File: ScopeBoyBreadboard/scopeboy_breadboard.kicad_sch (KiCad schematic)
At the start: 7 parts, among them U1 Opamp_Dual

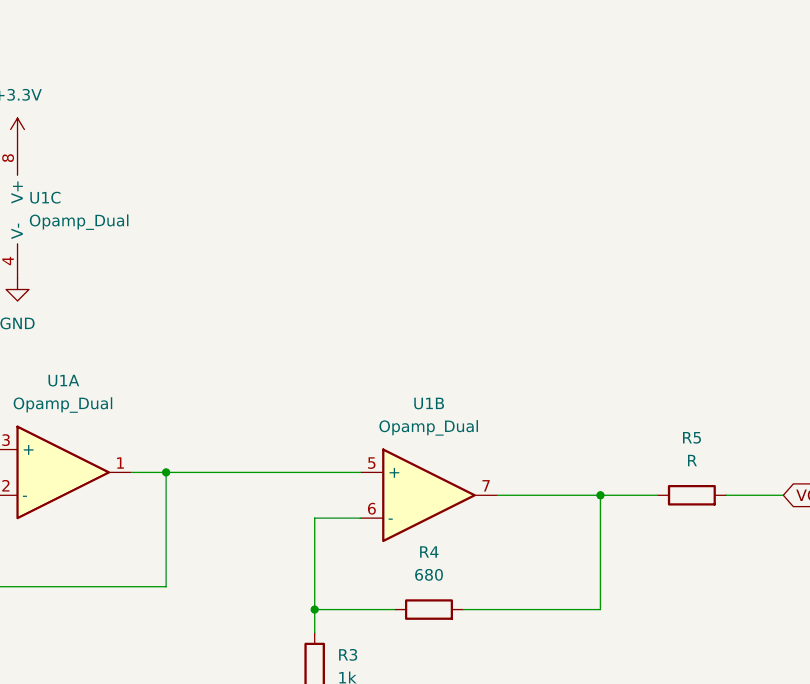
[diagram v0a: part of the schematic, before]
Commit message: Edited schematic, changed default trigger, and working on gain mode
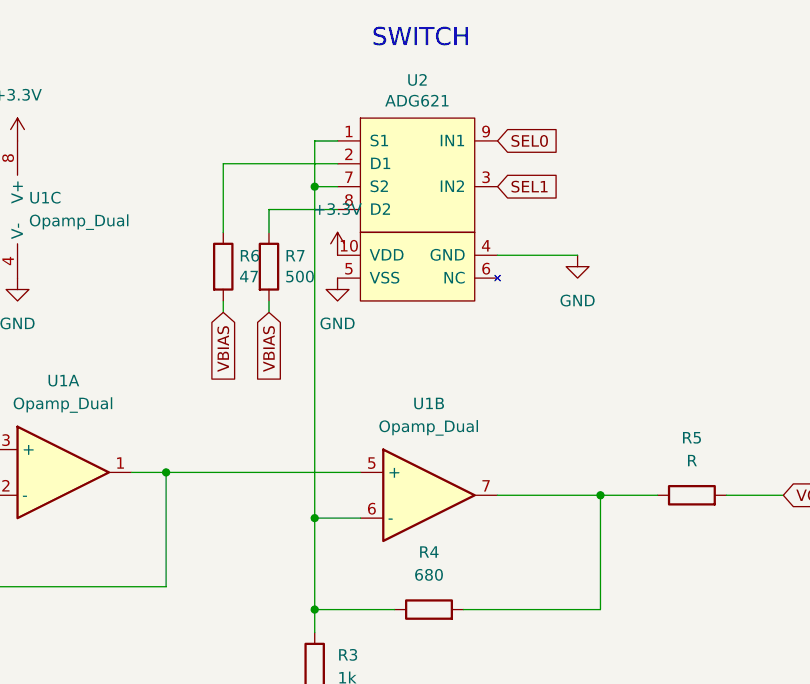
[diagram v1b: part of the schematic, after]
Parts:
- added R6: 47, Resistor_SMD:R_0603_1608Metric, symbol Device:R
- added R7: 500, Resistor_SMD:R_0603_1608Metric, symbol Device:R
- added U2: ADG621, Package_SO:MSOP-10_3x3mm_P0.5mm, symbol rpicoscope:ADG621
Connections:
- net +3.3V: now also U2.10 (VDD)
- net GND: now also U2.4 (GND), U2.5 (VSS)
- net VBIAS: now also R6.2, R7.2
- net at R3.1, R4.1, U1.6 (-): now also U2.1 (S1), U2.7 (S2)
- new net: R6.1, U2.2 (D1)
- new net: R7.1, U2.8 (D2)
- new net SEL0: U2.9 (IN1)
- new net SEL1: U2.3 (IN2)
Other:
- note added: "SWITCH"

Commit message: Updated schematic
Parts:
- added C2: 22pF, symbol Device:C
- added R10: 1M, symbol Device:R
- added R8: 680k, Resistor_SMD:R_0603_1608Metric, symbol Device:R
- added R9: 100k, Resistor_SMD:R_0603_1608Metric, symbol Device:R
- R5: value R -> 100
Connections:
- net VSIG is gone; now on net VBIAS: C1.1
- net GND: now also C2.2, R10.2, R9.1
- net VBIAS: now also C2.1, R10.1; no longer C1.2, U1.3 (+)
- new net: R8.2, R9.2, U1.3 (+)
- new net: C1.2, R8.1
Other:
- note added: "Cant measure too low frequency signals"
- moved on the sheet: R1, R2

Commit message: Updated schematic
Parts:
- added R11: 1MEG, Resistor_SMD:R_0603_1608Metric, symbol Device:R
- added R12: 22, Resistor_SMD:R_0603_1608Metric, symbol Device:R
- added U3: AD8561, Package_TO_SOT_SMD:SOT-23-6, symbol rpicoscope:TLV3501
- added U4: MCP4822, symbol Analog_DAC:MCP4822
- C1: value C -> 10n
- U1: value Opamp_Dual -> MCP6242
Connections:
- net +3.3V: now also U3.4, U4.7 (Vss)
- net GND: now also U3.2, U3.6, U4.1 (Vdd), U4.5 (~{LDAC})
- new net: R11.1, U3.3 (+)
- new net: R12.2, U3.5
- new net: U3.1 (-), U4.8 (VA)
- new net DAC_CS: U4.2 (~{CS})
- new net MOSI: U4.4 (SDI)
- new net SCLK: U4.3 (SCK)
- new net TRIG: R12.1
- new net VIN: R11.2
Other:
- note added: "Gain modes: -> Max Voltage (at 3.3V): LOW: 0.2153846154 LOW: 15.7V MEDIUM: 0.39000539 MEDIUM: 8.46V HIGH: 1.983087834 HIGH: 1.67V"
- note added: "Max Freq 70kHz"
- note added: "Min Freq In ~2kHz"
- note added: "TRIG"
- note removed: "Cant measure too low frequency signals"
- note removed: "TODO make the high gain have 1k EQ resistance and the low gain have 2k or 3k"
- company: (none) -> Cornell University
- title: (none) -> ScopeBoy Breadboard Version

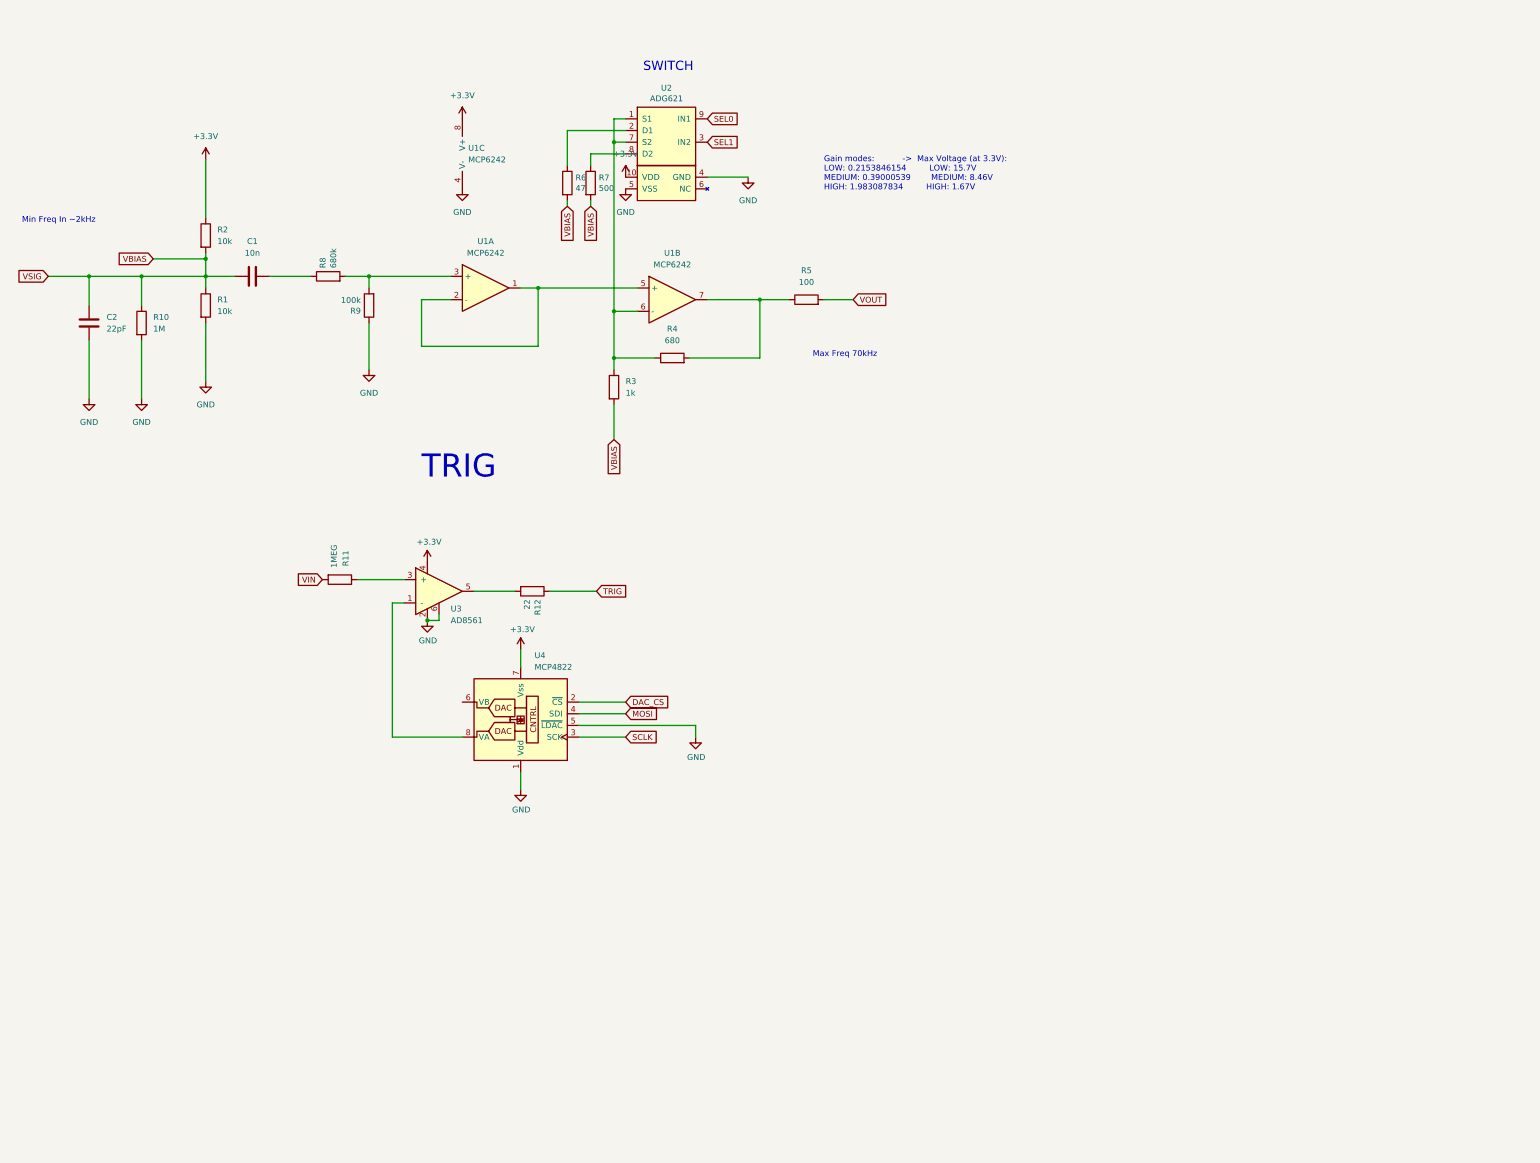
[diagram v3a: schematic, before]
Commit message: Fixed website include and added schematics
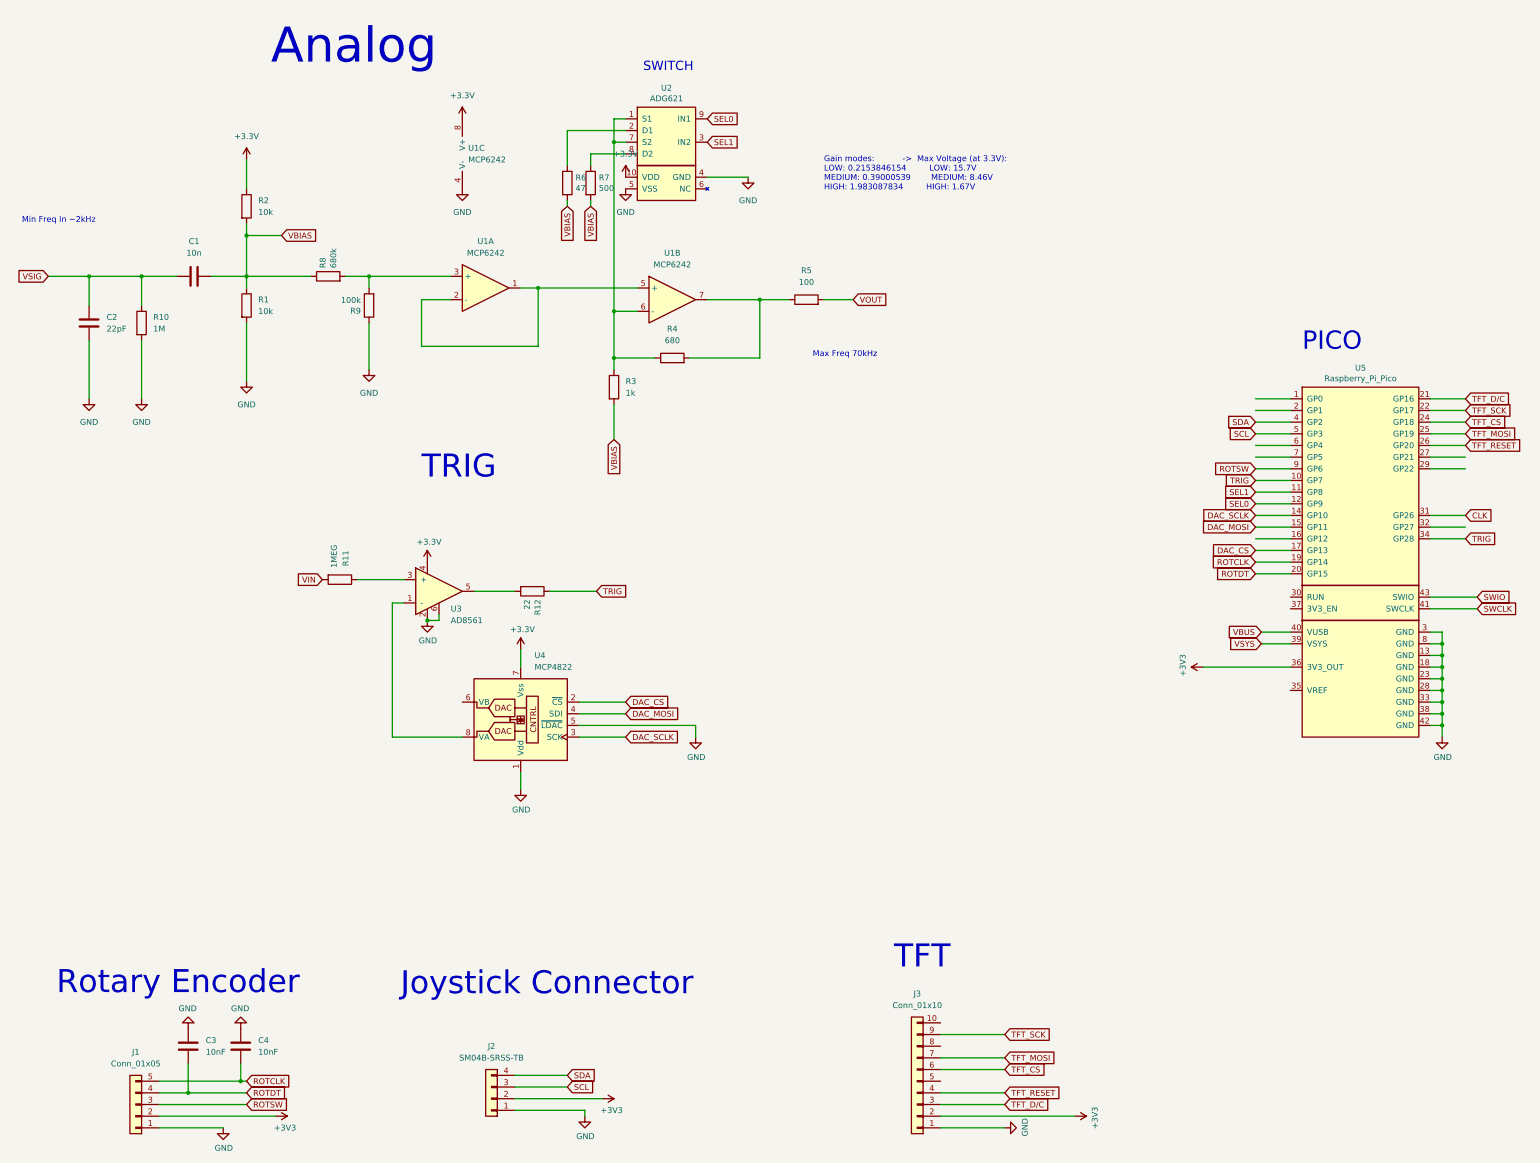
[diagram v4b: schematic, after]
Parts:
- added C3, C4: 10nF, Capacitor_SMD:C_0603_1608Metric, symbol Device:C
- added J1: Conn_01x05, Connector_PinHeader_2.54mm:PinHeader_1x05_P2.54mm_Vertical, symbol Connector_Generic:Conn_01x05
- added J2: SM04B-SRSS-TB, Connector_JST:JST_SH_SM04B-SRSS-TB_1x04-1MP_P1.00mm_Horizontal, symbol Connector_Generic:Conn_01x04
- added J3: Conn_01x10, Connector_PinHeader_2.54mm:PinHeader_1x10_P2.54mm_Vertical, symbol Connector_Generic:Conn_01x10
- added U5: Raspberry_Pi_Pico, RPi_Pico:RPi_Pico_SMD_TH, symbol rpicoscope:Raspberry_Pi_Pico
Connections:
- net DAC_CS: now also U5.17 (GP13)
- net GND: now also C3.1, C4.1, J1.1 (Pin_1), J2.1 (Pin_1), J3.1 (Pin_1), U5.13 (GND), U5.18 (GND), U5.23 (GND), U5.28 (GND), U5.3 (GND), U5.33 (GND), U5.38 (GND), U5.42 (GND), U5.8 (GND)
- net SEL0: now also U5.12 (GP9)
- net SEL1: now also U5.11 (GP8)
- net TRIG: now also U5.10 (GP7), U5.34 (GP28)
- net VBIAS: now also C1.2, R8.1; no longer C1.1, C2.1, R10.1
- net MOSI renamed DAC_MOSI
- net DAC_MOSI: now also U5.15 (GP11)
- net SCLK renamed DAC_SCLK
- net DAC_SCLK: now also U5.14 (GP10)
- new net +3V3: J1.2 (Pin_2), J2.2 (Pin_2), J3.2 (Pin_2), U5.36 (3V3_OUT)
- new net CLK: U5.31 (GP26)
- new net ROTCLK: C4.2, J1.5 (Pin_5), U5.19 (GP14)
- new net ROTDT: C3.2, J1.4 (Pin_4), U5.20 (GP15)
- new net ROTSW: J1.3 (Pin_3), U5.9 (GP6)
- new net SCL: J2.3 (Pin_3), U5.5 (GP3)
- new net SDA: J2.4 (Pin_4), U5.4 (GP2)
- new net SWCLK: U5.41 (SWCLK)
- new net SWIO: U5.43 (SWIO)
- new net TFT_CS: J3.6 (Pin_6), U5.24 (GP18)
- new net TFT_D/C: J3.3 (Pin_3), U5.21 (GP16)
- new net TFT_MOSI: J3.7 (Pin_7), U5.25 (GP19)
- new net TFT_RESET: J3.4 (Pin_4), U5.26 (GP20)
- new net TFT_SCK: J3.9 (Pin_9), U5.22 (GP17)
- new net VBUS: U5.40 (VUSB)
- new net VSIG: C1.1, C2.1, R10.1
- new net VSYS: U5.39 (VSYS)
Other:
- note added: "Analog"
- note added: "Joystick Connector"
- note added: "PICO"
- note added: "Rotary Encoder"
- note added: "TFT"
- moved on the sheet: C1, R1, R2
